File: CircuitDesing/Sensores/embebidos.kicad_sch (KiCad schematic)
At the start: 15 parts

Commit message: Coversores lógicos + alertas + cambios genrales
Coversores lógicos + alertas + cambios generales
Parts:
- removed HMI1: Conn_01x07, Connector_JST:JST_EH_B7B-EH-A_1x07_P2.50mm_Vertical, symbol Connector_Generic:Conn_01x07
- removed RCL3, RDA3: 10k, Resistor_SMD:R_0805_2012Metric_Pad1.20x1.40mm_HandSolder, symbol Device:R
- removed Temp&Humi1: Conn_01x03, Connector_JST:JST_EH_B3B-EH-A_1x03_P2.50mm_Vertical, symbol Connector_Generic:Conn_01x03
- added Botones_M: Conn_01x03, Connector_JST:JST_EH_B3B-EH-A_1x03_P2.50mm_Vertical, symbol Connector_Generic:Conn_01x03
- added Buzzer, LedRojo, LedVerde: Conn_01x02, symbol Connector_Generic:Conn_01x02
- added C-Actuadores: Conn_01x05, symbol Connector_Generic:Conn_01x05
- added Q?: BSS138, Package_TO_SOT_SMD:SOT-23, symbol Transistor_FET:BSS138
- added R_p2: 47, Resistor_SMD:R_0805_2012Metric_Pad1.20x1.40mm_HandSolder, symbol Device:R
- added R_p3: 1k, symbol Device:R
- added Rb: 1k, Resistor_SMD:R_0603_1608Metric_Pad0.98x0.95mm_HandSolder, symbol Device:R
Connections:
- net 3.3v: now also Botones_M.1 (Pin_1)
- net Buzzer: now also Rb.2
- net C_hum: now also C-Actuadores.4 (Pin_4)
- net GND: now also Botones_M.3 (Pin_3), C-Actuadores.5 (Pin_5), LedVerde.2 (Pin_2), Q?.2 (S)
- new net: LedRojo.1 (Pin_1), R_p3.2
- new net: LedVerde.1 (Pin_1), R_p2.1
- new net: Buzzer.2 (Pin_2), LedRojo.2 (Pin_2), Q?.3 (D)
- new net: Q?.1 (G), Rb.1
- new net +3V3: Buzzer.1 (Pin_1), R_p3.1
- new net Botones: Botones_M.2 (Pin_2)
- new net C_ilum: C-Actuadores.1 (Pin_1)
- new net C_temp1: C-Actuadores.2 (Pin_2)
- new net C_temp2: C-Actuadores.3 (Pin_3)
- new net Led_Verde: R_p2.2
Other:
- note added: "Alertas"
- moved on the sheet: Iluminación1, JI2C2, J_I2C1, J_prog1, L_p1, RCL1, RCL2, RDA1, RDA2, RIEGO1, R_p1

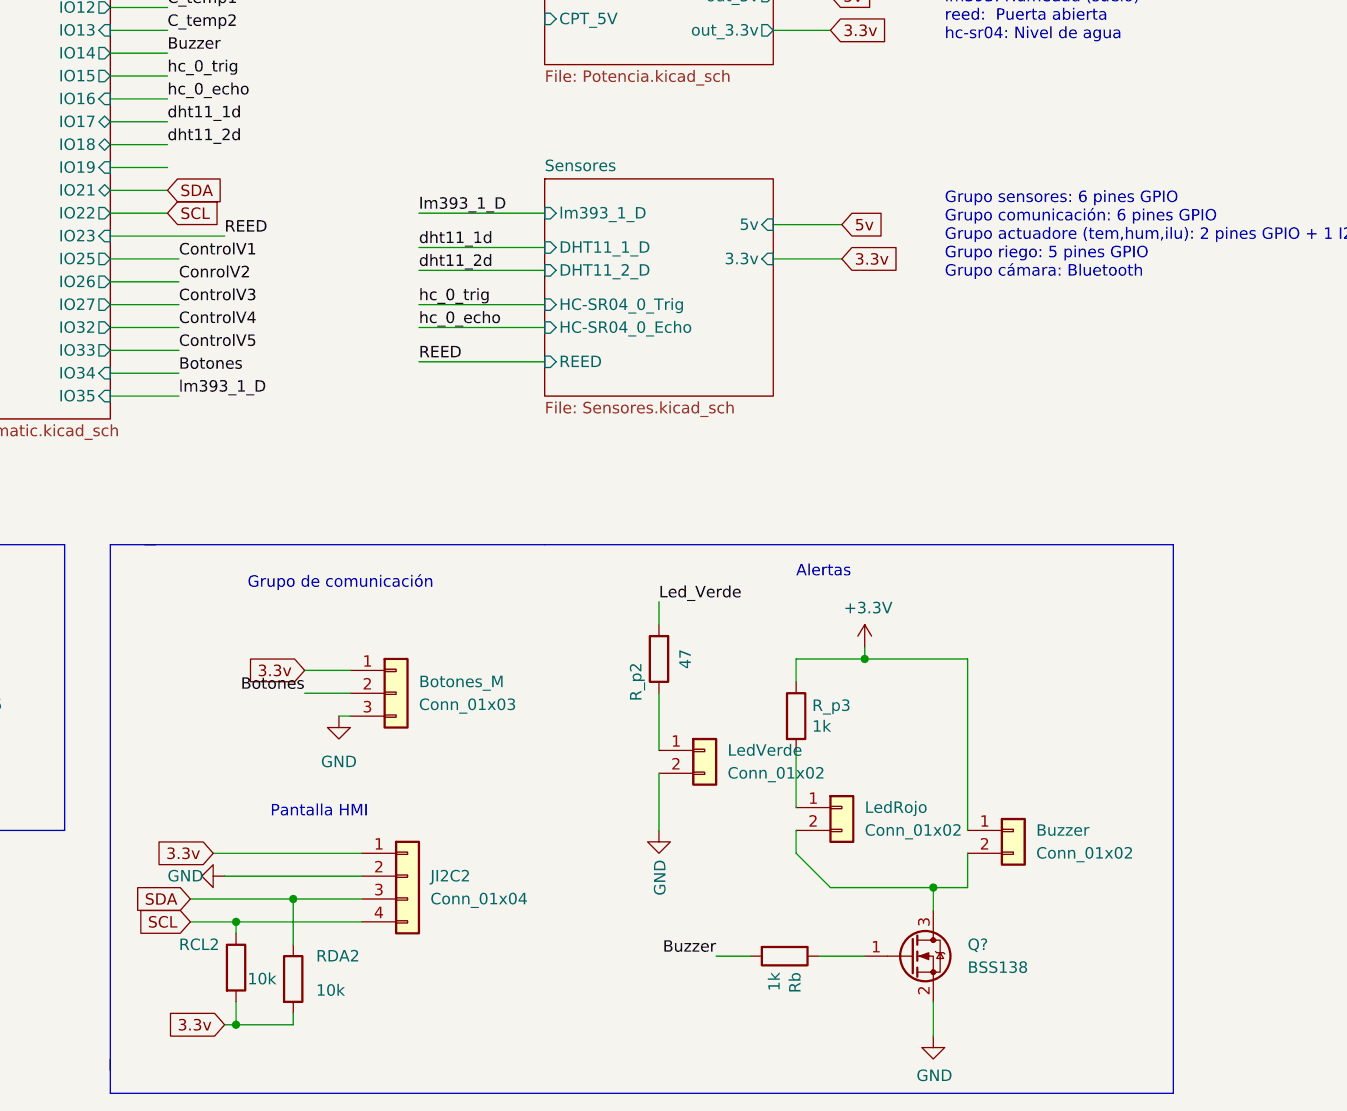
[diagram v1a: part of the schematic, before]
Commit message: Cambio 3.3V en alertas
Cambio 3.3V en alertas
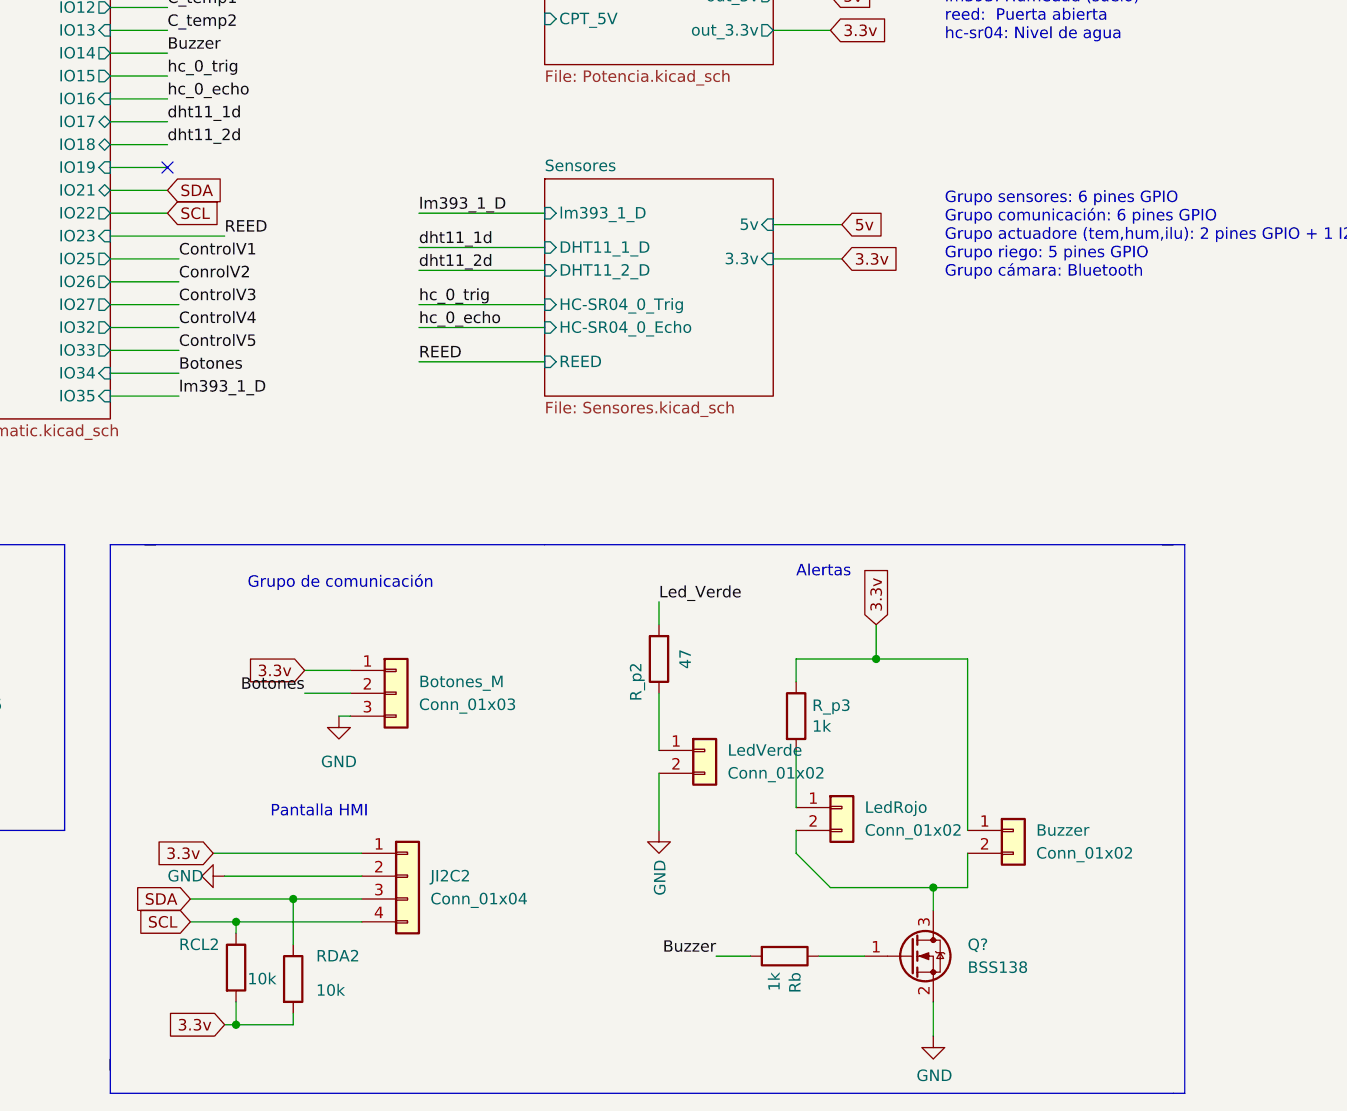
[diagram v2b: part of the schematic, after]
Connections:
- net +3V3 is gone; now on net 3.3v: Buzzer.1 (Pin_1), R_p3.1
- no-connect marks 3 -> 4
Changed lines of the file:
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@@
   (junction (at 39.37 30.48) (diameter 0) (color 0 0 0 0)
   )
-  (junction (at 201.93 116.84) (diameter 0) (color 0 0 0 0)
+  (junction (at 203.2 116.84) (diameter 0) (color 0 0 0 0)
   )
   (junction (at 132.08 157.48) (diameter 0) (color 0 0 0 0)
@@
   )
   (no_connect (at 31.75 71.12))
+  (no_connect (at 124.46 62.23))
   (no_connect (at 31.75 58.42))
   (no_connect (at 31.75 60.96))
@@
     (stroke (width 0) (type default) (color 0 0 0 0))
   )
+  (polyline (pts (xy 234.95 104.14) (xy 237.49 104.14))
+    (stroke (width 0) (type default) (color 0 0 0 0))
+  )
+  (polyline (pts (xy 236.22 165.1) (xy 237.49 165.1))
+    (stroke (width 0) (type default) (color 0 0 0 0))
+  )
   (wire (pts (xy 213.36 116.84) (xy 213.36 135.89))
     (stroke (width 0) (type default) (color 0 0 0 0))
@@
     (stroke (width 0) (type default) (color 0 0 0 0))
   )
+  (polyline (pts (xy 237.49 104.14) (xy 237.49 165.1))
+    (stroke (width 0) (type default) (color 0 0 0 0))
+  )
   (wire (pts (xy 44.45 120.65) (xy 36.83 120.65))
     (stroke (width 0) (type default) (color 0 0 0 0))
@@
     (stroke (width 0) (type default) (color 0 0 0 0))
   )
+  (wire (pts (xy 203.2 113.03) (xy 203.2 116.84))
+    (stroke (width 0) (type default) (color 0 0 0 0))
+  )
   (polyline (pts (xy 16.51 104.14) (xy 19.05 104.14))
     (stroke (width 0) (type default) (color 0 0 0 0))
@@
     (stroke (width 0) (type default) (color 0 0 0 0))
   )
+  (wire (pts (xy 203.2 116.84) (xy 213.36 116.84))
+    (stroke (width 0) (type default) (color 0 0 0 0))
+  )
   (wire (pts (xy 132.08 146.05) (xy 146.05 146.05))
     (stroke (width 0) (type default) (color 0 0 0 0))
@@
     (stroke (width 0) (type default) (color 0 0 0 0))
   )
-  (wire (pts (xy 201.93 115.57) (xy 201.93 116.84))
-    (stroke (width 0) (type default) (color 0 0 0 0))
-  )
   (wire (pts (xy 191.77 68.58) (xy 199.39 68.58))
     (stroke (width 0) (type default) (color 0 0 0 0))
@@
     (stroke (width 0) (type default) (color 0 0 0 0))
   )
-  (wire (pts (xy 213.36 116.84) (xy 201.93 116.84))
-    (stroke (width 0) (type default) (color 0 0 0 0))
-  )
   (wire (pts (xy 62.23 76.2) (xy 62.23 84.455))
     (stroke (width 0) (type default) (color 0 0 0 0))
@@
     (stroke (width 0) (type default) (color 0 0 0 0))
   )
-  (polyline (pts (xy 236.22 104.14) (xy 236.22 165.1))
-    (stroke (width 0) (type default) (color 0 0 0 0))
-  )
   (wire (pts (xy 118.11 82.55) (xy 125.73 82.55))
     (stroke (width 0) (type default) (color 0 0 0 0))
@@
     (stroke (width 0) (type default) (color 0 0 0 0))
   )
-  (wire (pts (xy 201.93 116.84) (xy 194.31 116.84))
+  (wire (pts (xy 194.31 116.84) (xy 203.2 116.84))
     (stroke (width 0) (type default) (color 0 0 0 0))
   )
@@
     )
   )
+  (global_label "3.3v" (shape input) (at 203.2 113.03 90) (fields_autoplaced)
+    (effects (font (size 1.27 1.27)) (justify left))
+    (property "Intersheet References" "${INTERSHEET_REFS}" (id 0) (at 203.1206 106.6255 90)
+      (effects (font (size 1.27 1.27)) (justify left) hide)
+    )
+  )
   (global_label "3.3v" (shape input) (at 139.7 118.11 180) (fields_autoplaced)
     (effects (font (size 1.27 1.27)) (justify right))
@@
       (effects (font (size 1.27 1.27)) (justify right) hide)
     )
-  )
-  (symbol (lib_id "DiseñoApp-rescue:+3.3V-power") (at 201.93 115.57 0) (unit 1)
-    (in_bom yes) (on_board yes)
-    (property "Reference" "#PWR?" (id 0) (at 201.93 119.38 0)
-      (effects (font (size 1.27 1.27)) hide)
-    )
-    (property "Value" "+3.3V" (id 1) (at 202.311 111.1758 0))
-    (property "Footprint" "" (id 2) (at 201.93 115.57 0)
-      (effects (font (size 1.27 1.27)) hide)
-    )
-    (property "Datasheet" "" (id 3) (at 201.93 115.57 0)
-      (effects (font (size 1.27 1.27)) hide)
-    )
-    (pin "1")
   )
   (symbol (lib_id "power:GND") (at 33.02 68.58 90) (unit 1)
@@
       (reference "#PWR0118") (unit 1) (value "GND") (footprint "")
     )
-    (path "/116e1c6b-b3c1-414e-8400-020455f473bb"
-      (reference "#PWR?") (unit 1) (value "+3.3V") (footprint "")
-    )
     (path "/871c1e73-85f5-4c5a-9fae-943eb3527b63"

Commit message: Ruteo2.0
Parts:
- removed J_prog1: Conn_01x06_Male, Connector_PinHeader_2.54mm:PinHeader_1x06_P2.54mm_Horizontal, symbol Connector:Conn_01x06_Male
- added J1: Conn_01x03_Male, Connector_PinHeader_2.54mm:PinHeader_1x03_P2.54mm_Vertical, symbol Connector:Conn_01x03_Male
- Buzzer1: renamed from Buzzer; footprint (none) -> Connector_JST:JST_EH_B2B-EH-A_1x02_P2.50mm_Vertical
- C-Actuadores1: renamed from C-Actuadores; footprint (none) -> Connector_JST:JST_EH_B5B-EH-A_1x05_P2.50mm_Vertical
- LedRojo1: renamed from LedRojo; footprint (none) -> Connector_JST:JST_EH_B2B-EH-A_1x02_P2.50mm_Vertical
- LedVerde1: renamed from LedVerde; footprint (none) -> Connector_JST:JST_EH_B2B-EH-A_1x02_P2.50mm_Vertical
- R_p3: footprint (none) -> Resistor_SMD:R_0805_2012Metric_Pad1.20x1.40mm_HandSolder
- gave numbers to parts that had none: 1
- renumbered Botones_M to Botones_M1, JI2C2 to JI2C1, Rb to Rb1
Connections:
- net GND: now also J1.3 (Pin_3)
- net Prog_Rx: now also J1.1 (Pin_1)
- net Prog_Tx: now also J1.2 (Pin_2)
- no-connect marks 4 -> 1
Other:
- sheet Sensores ports: added HC-SR04Echo, HC-SR04Trig; removed HC-SR04_0_Echo, HC-SR04_0_Trig
- moved on the sheet: LedVerde1, R_p2

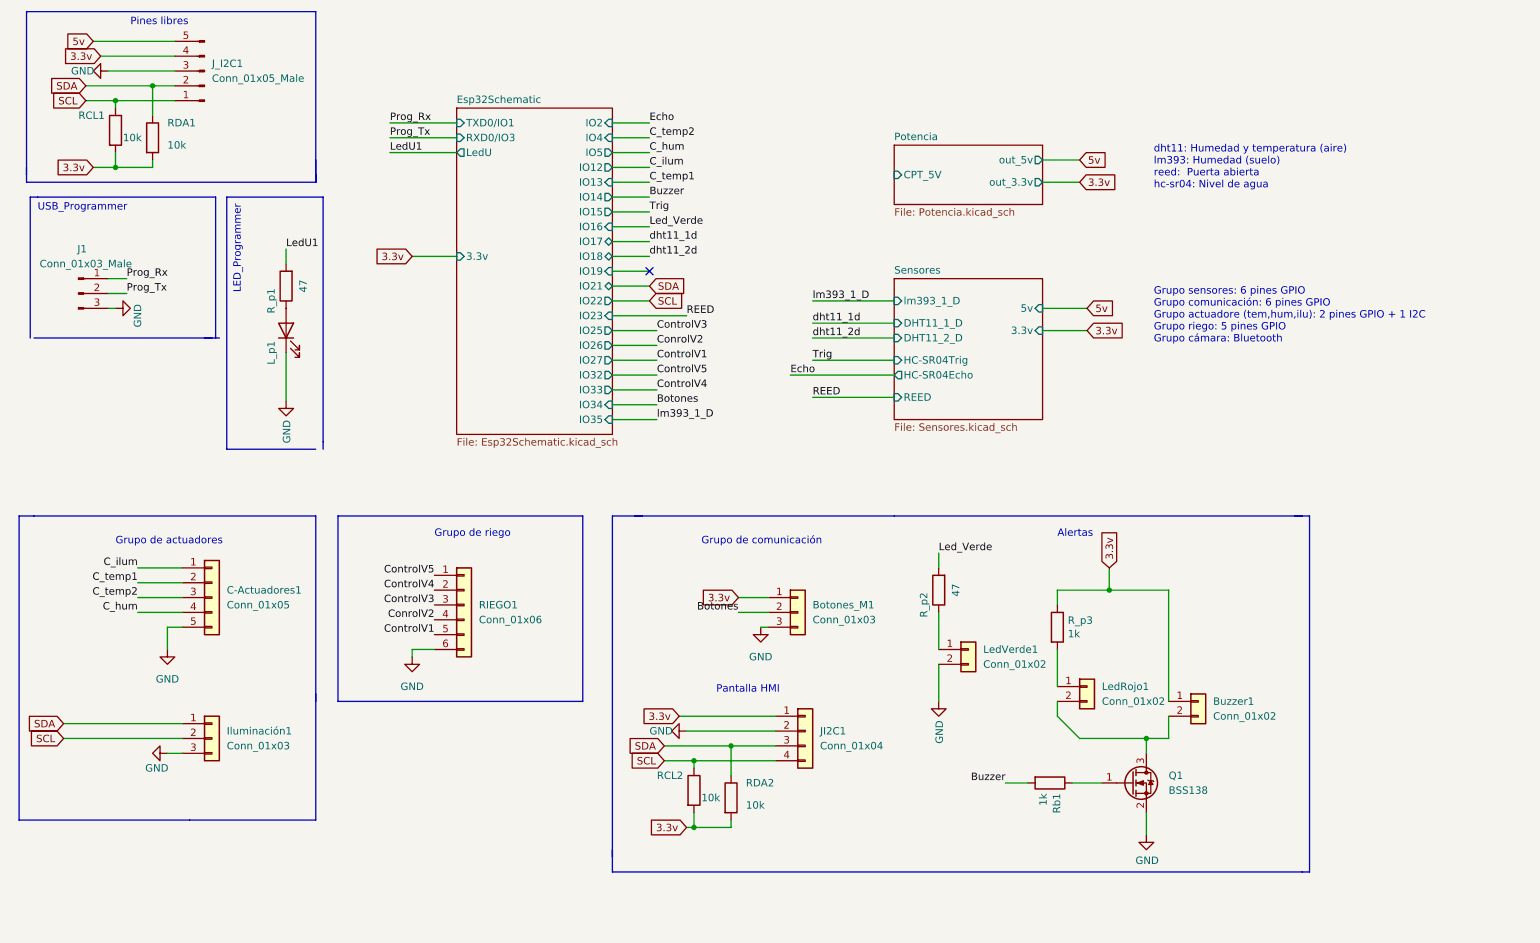
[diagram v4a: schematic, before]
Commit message: Ruteo plano de tierra
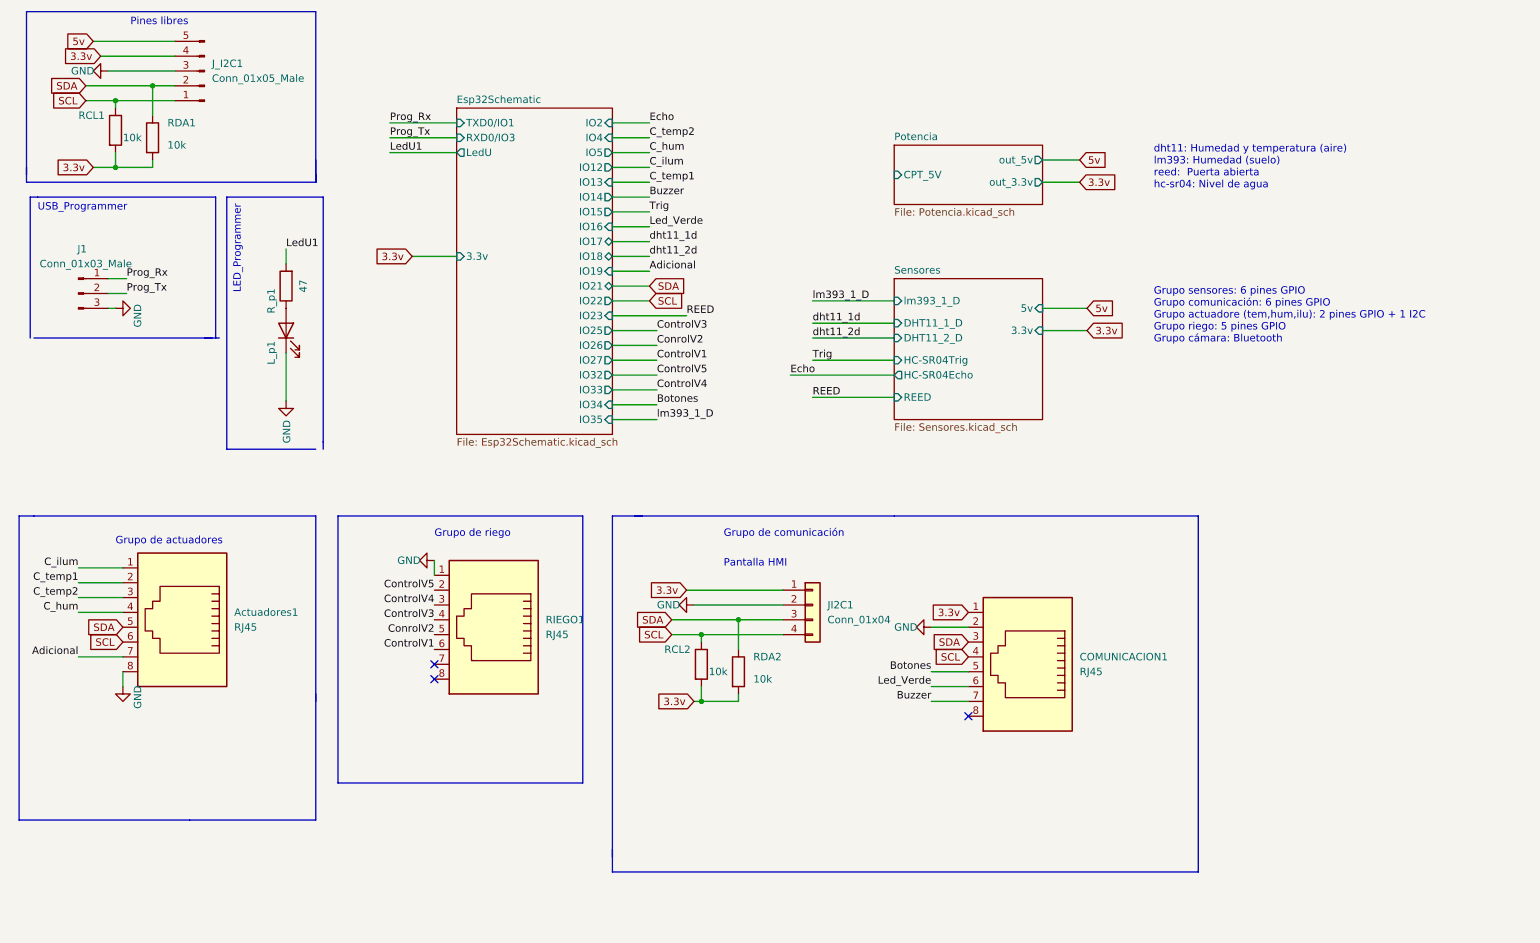
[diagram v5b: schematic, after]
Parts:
- removed Botones_M1, Iluminación1: Conn_01x03, Connector_JST:JST_EH_B3B-EH-A_1x03_P2.50mm_Vertical, symbol Connector_Generic:Conn_01x03
- removed Buzzer1, LedRojo1, LedVerde1: Conn_01x02, Connector_JST:JST_EH_B2B-EH-A_1x02_P2.50mm_Vertical, symbol Connector_Generic:Conn_01x02
- removed C-Actuadores1: Conn_01x05, Connector_JST:JST_EH_B5B-EH-A_1x05_P2.50mm_Vertical, symbol Connector_Generic:Conn_01x05
- removed Q1: BSS138, Package_TO_SOT_SMD:SOT-23, symbol Transistor_FET:BSS138
- removed RIEGO1: Conn_01x06, Connector_JST:JST_EH_B6B-EH-A_1x06_P2.50mm_Vertical, symbol Connector_Generic:Conn_01x06
- removed R_p2: 47, Resistor_SMD:R_0805_2012Metric_Pad1.20x1.40mm_HandSolder, symbol Device:R
- removed R_p3: 1k, Resistor_SMD:R_0805_2012Metric_Pad1.20x1.40mm_HandSolder, symbol Device:R
- removed Rb1: 1k, Resistor_SMD:R_0603_1608Metric_Pad0.98x0.95mm_HandSolder, symbol Device:R
- added Actuadores1, COMUNICACION1, RIEGO1: RJ45, Connector_RJ:RJ45_Amphenol_54602-x08_Horizontal, symbol Connector:RJ45
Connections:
- net 3.3v: now also COMUNICACION1.1
- net Botones: now also COMUNICACION1.5
- net Buzzer: now also COMUNICACION1.7
- net C_hum: now also Actuadores1.4
- net C_ilum: now also Actuadores1.1
- net C_temp1: now also Actuadores1.2
- net C_temp2: now also Actuadores1.3
- net ConrolV2: now also RIEGO1.5
- net ControlV1: now also RIEGO1.6
- net ControlV3: now also RIEGO1.4
- net ControlV4: now also RIEGO1.3
- net ControlV5: now also RIEGO1.2
- net GND: now also Actuadores1.8, COMUNICACION1.2, RIEGO1.1
- net Led_Verde: now also COMUNICACION1.6
- net SCL: now also Actuadores1.6, COMUNICACION1.4
- net SDA: now also Actuadores1.5, COMUNICACION1.3
- new net Adicional: Actuadores1.7
- no-connect marks 1 -> 3
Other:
- note removed: "Alertas"
- moved on the sheet: JI2C1, RCL2, RDA2
